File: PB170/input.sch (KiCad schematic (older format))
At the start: 0 parts

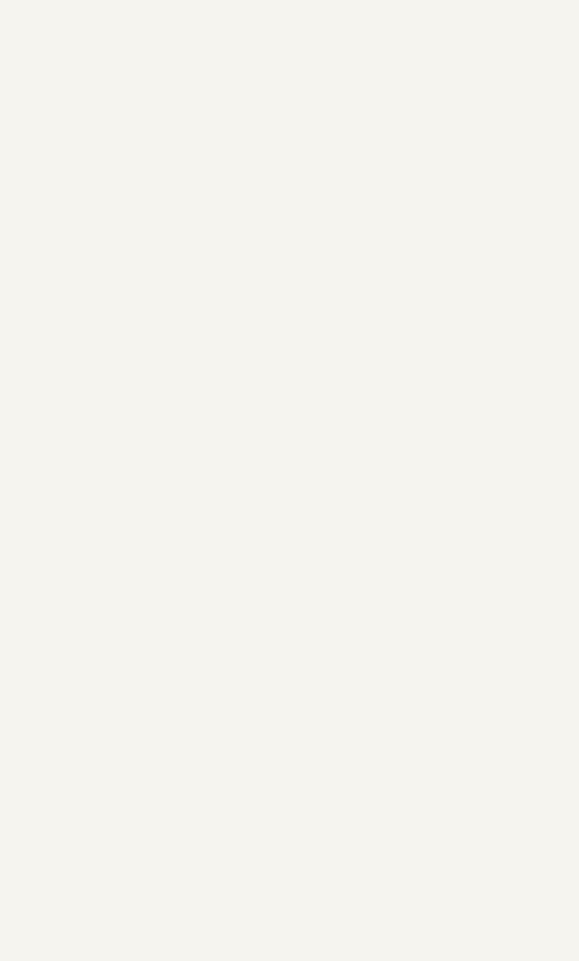
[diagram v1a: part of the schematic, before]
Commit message: Remove xor from the main sheet
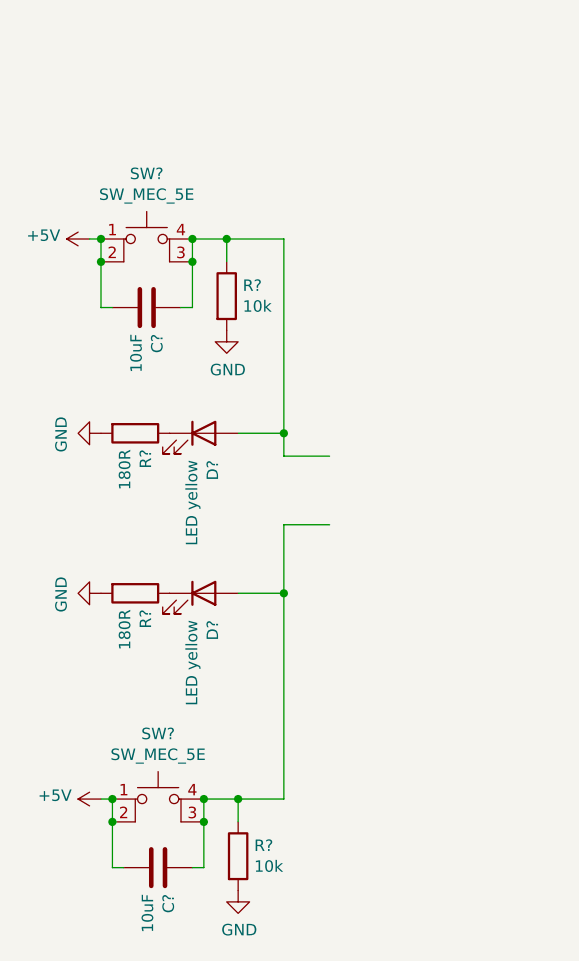
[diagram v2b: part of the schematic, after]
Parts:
- added C? (x2): 10uF, Capacitors_SMD:C_0805, symbol Device:C
- added D? (x2): LED yellow, LEDs:LED_0603, symbol Device:LED
- added R? (x2): 180R, Resistors_SMD:R_0603, symbol Device:R
- added R? (x2): 10k, Resistors_SMD:R_0603, symbol Device:R
- added SW? (x2): SW_MEC_5E, PB170:TactileSwitch_C381064, symbol Switch:SW_MEC_5E
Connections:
- net labels added: +5V, GND
- wire segments 0 -> 28

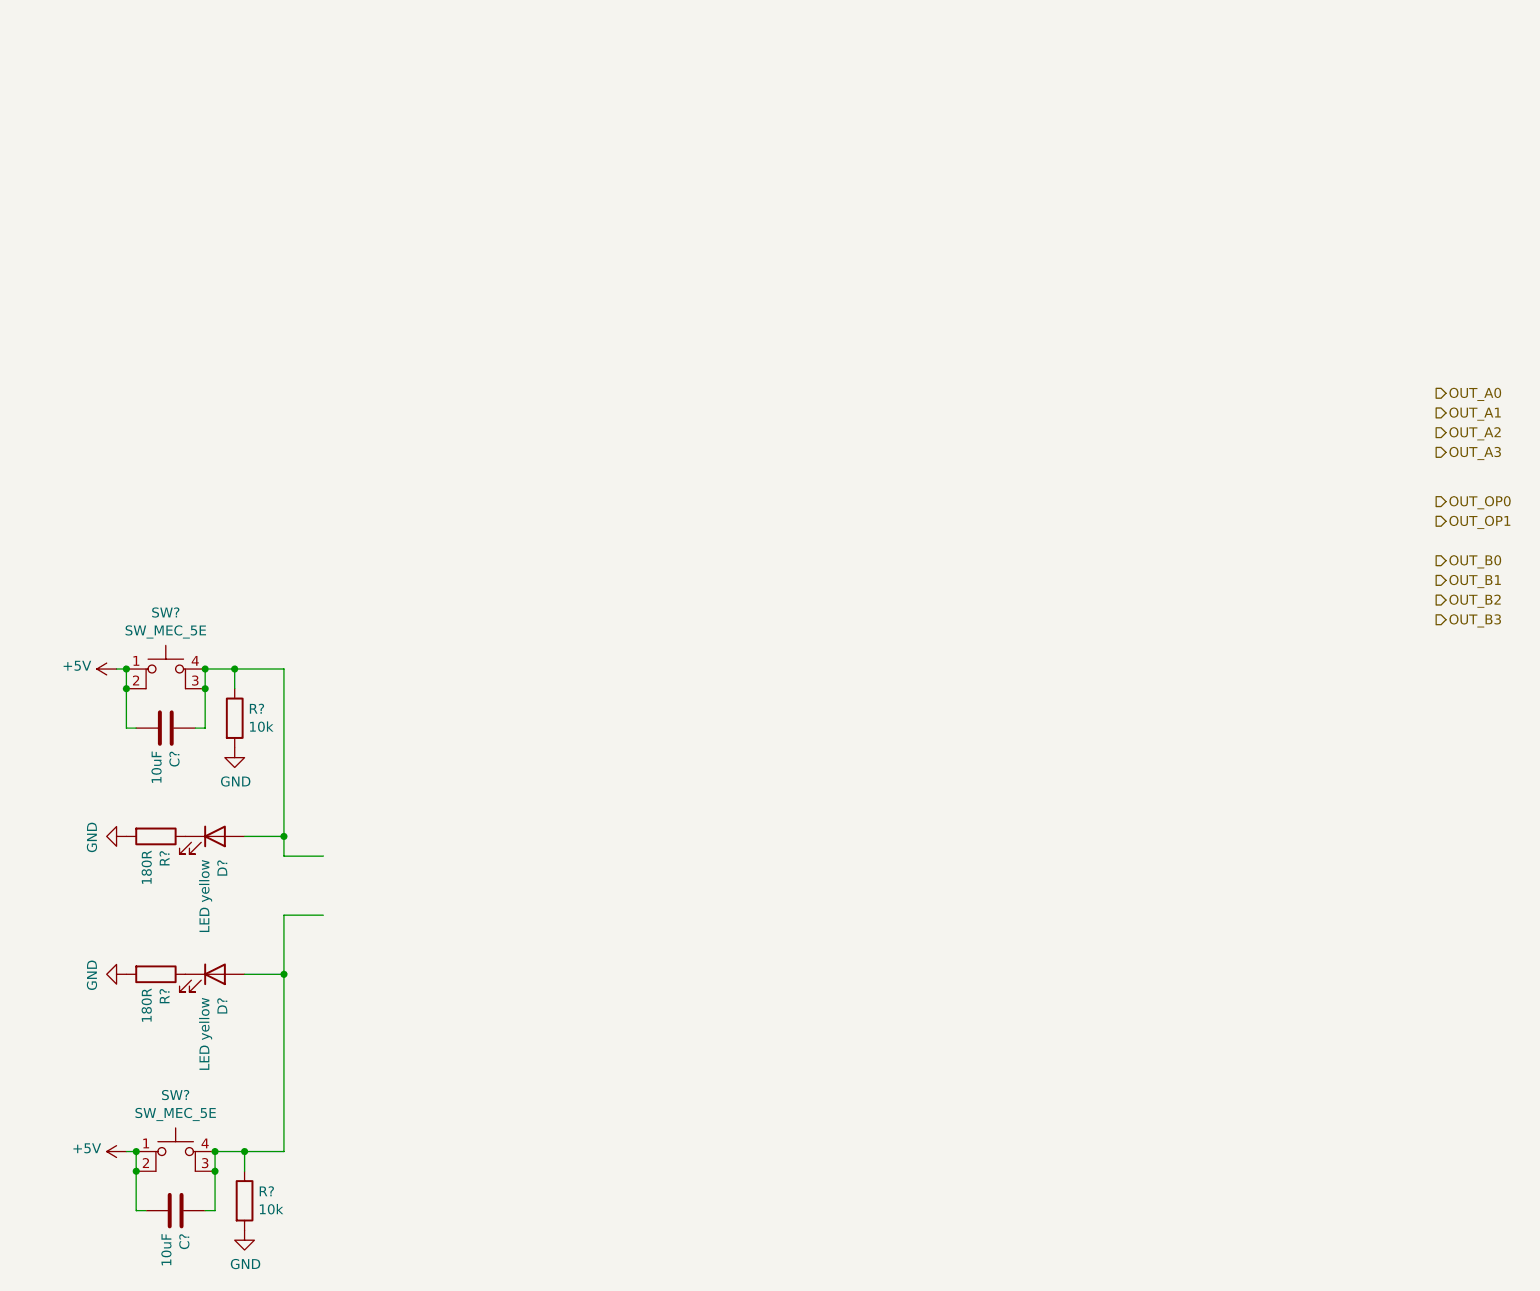
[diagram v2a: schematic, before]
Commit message: added switching buttons
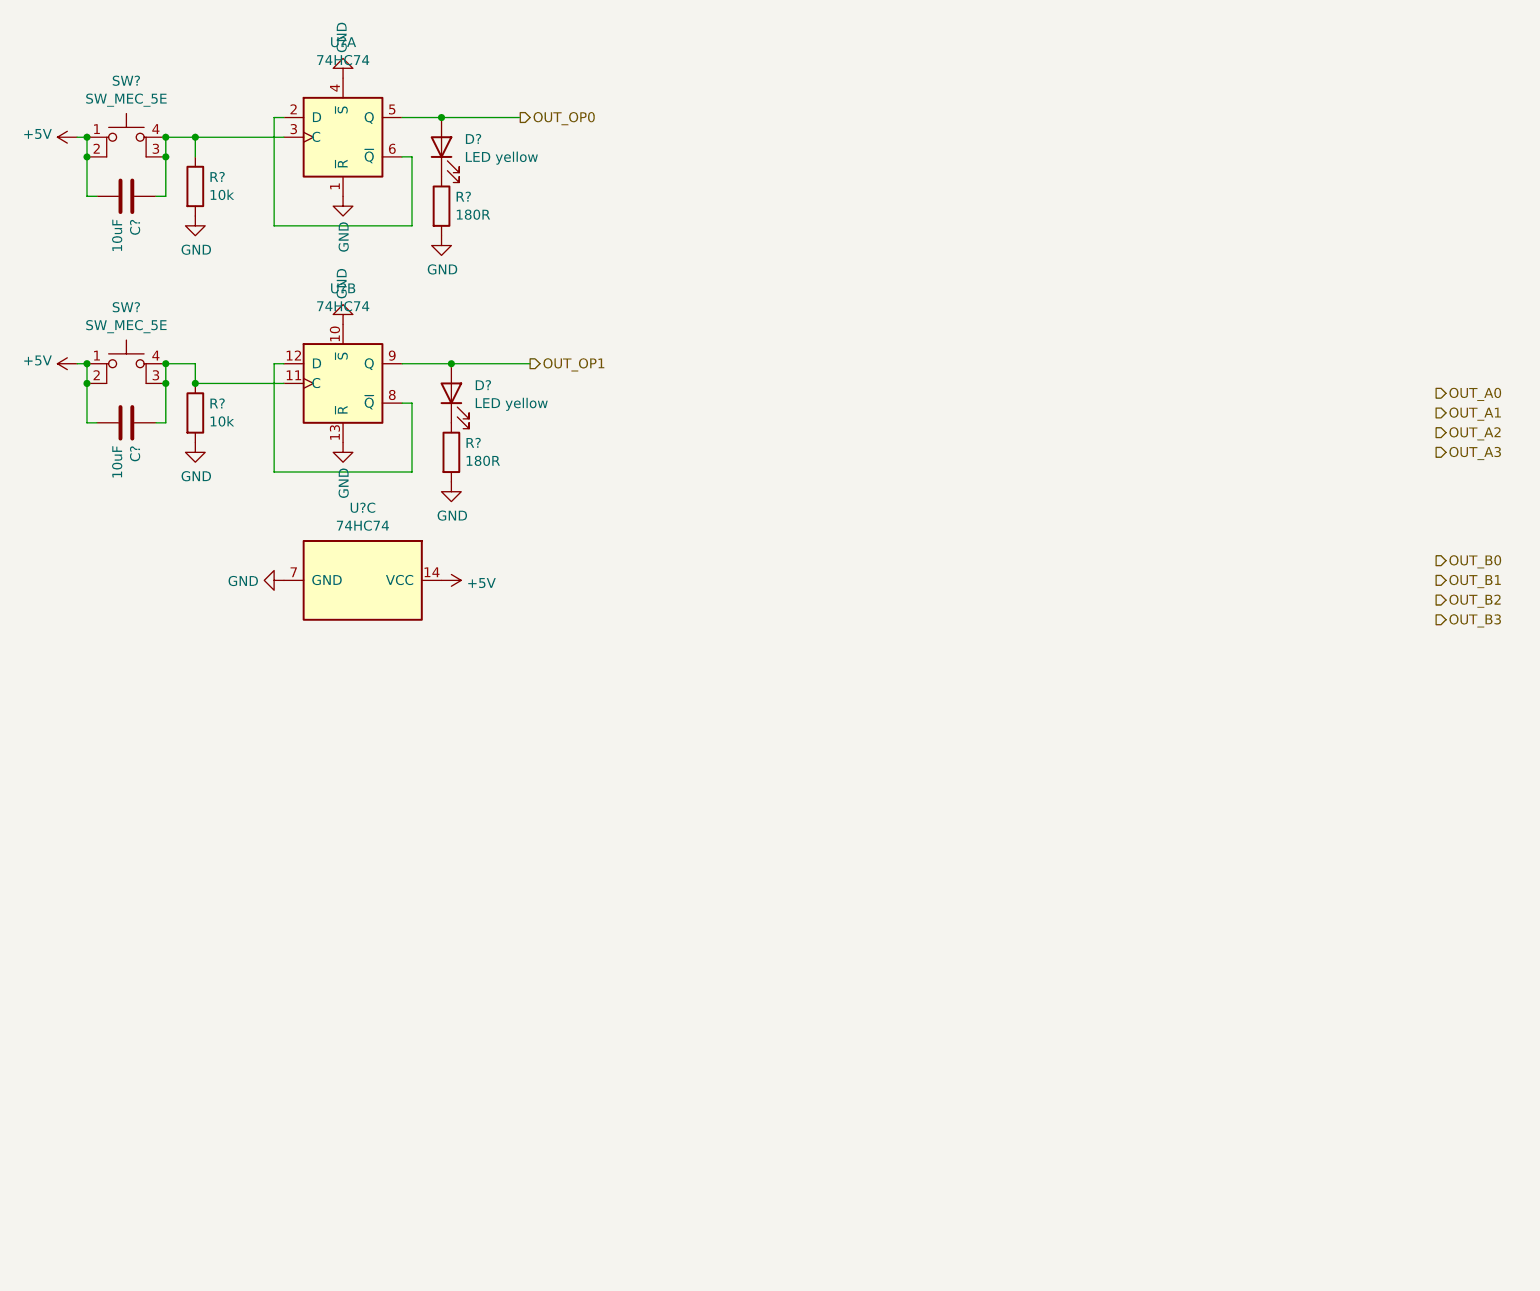
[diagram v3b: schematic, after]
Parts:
- added U? (x3): 74HC74, Package_SO:TSSOP-14_4.4x5mm_P0.65mm, symbol 74xx:74HC74
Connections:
- wire segments 28 -> 34
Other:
- moved on the sheet: C?, D?, R?, SW?
